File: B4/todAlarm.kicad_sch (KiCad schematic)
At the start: 4 parts, among them U407 74HC377, U408 74HC377, U409 74HC377, U410 74HC377

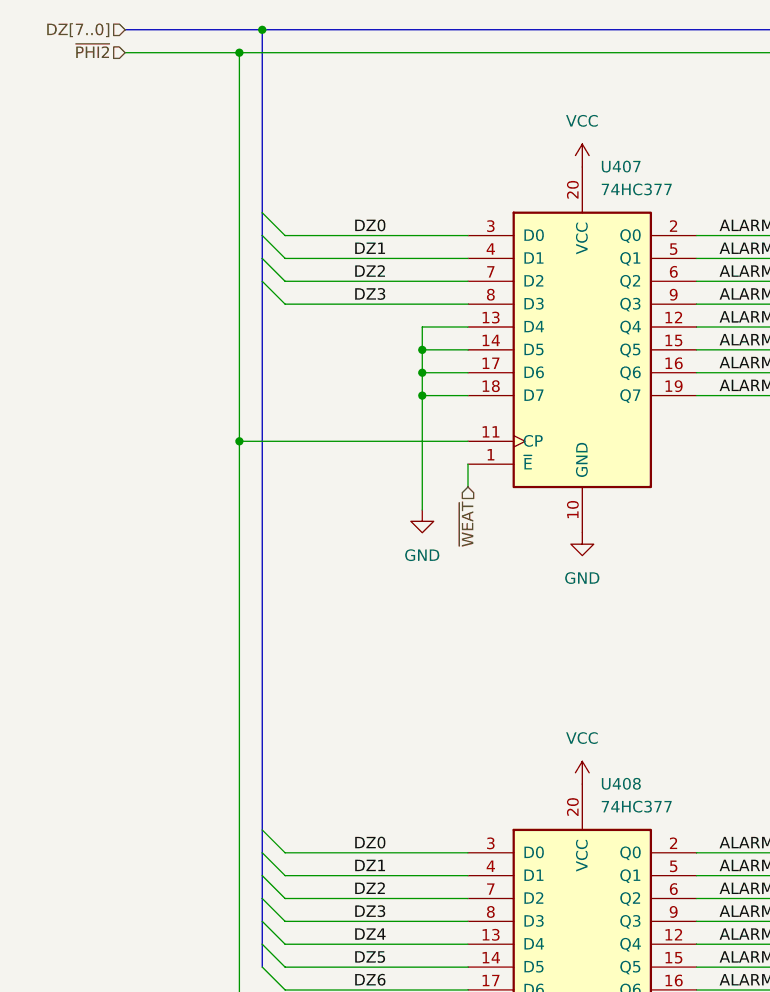
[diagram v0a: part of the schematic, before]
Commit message: B2 refactored. B4 Added. TOD sch completed.
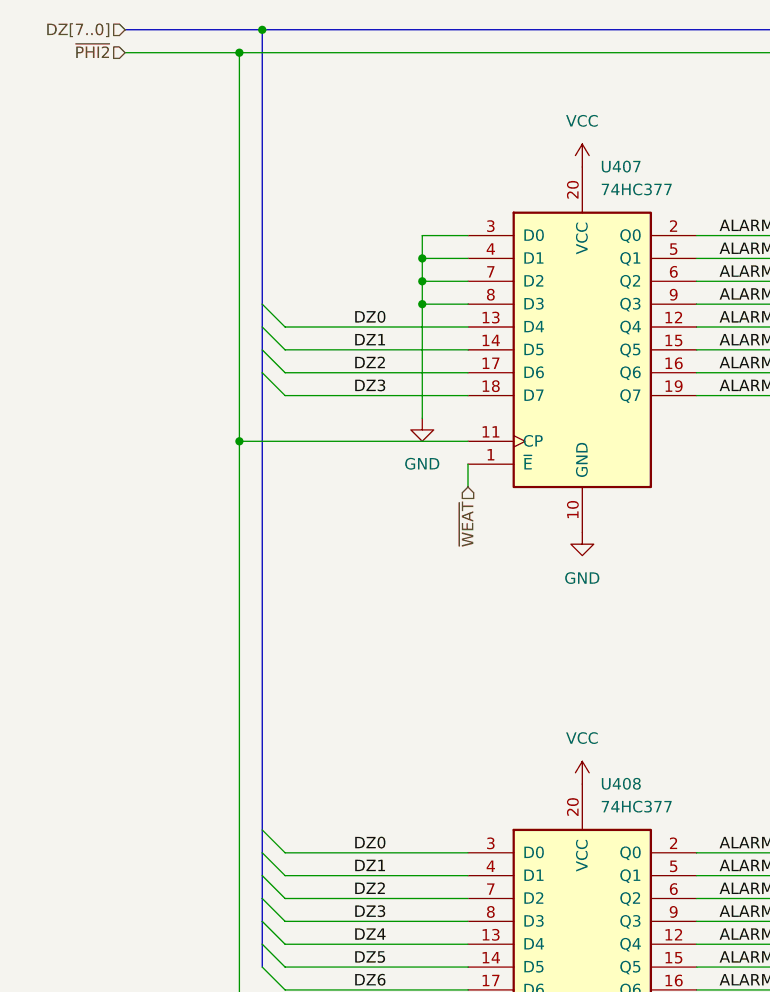
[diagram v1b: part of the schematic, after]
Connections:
- net DZ0: now also U407.13 (D4); no longer U407.3 (D0)
- net DZ1: now also U407.14 (D5); no longer U407.4 (D1)
- net DZ2: now also U407.17 (D6); no longer U407.7 (D2)
- net DZ3: now also U407.18 (D7); no longer U407.8 (D3)
- net GND: now also U407.3 (D0), U407.4 (D1), U407.7 (D2), U407.8 (D3); no longer U407.13 (D4), U407.14 (D5), U407.17 (D6), U407.18 (D7)

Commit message: TOD is here
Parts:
- renumbered U407 to U401
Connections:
- net ALARM0 is gone; now on net ALARM5: U401.2 (Q0)
- net ALARM1 is gone; now on net ALARM4: U401.5 (Q1)
- net ALARM2 is gone; now on net ALARM6: U401.6 (Q2)
- net ALARM3 is gone; now on net ALARM7: U401.9 (Q3)
- net ALARM30 is gone; now on net ALARM28: U410.16 (Q6)
- net ALARM12: now also U409.16 (Q6); no longer U409.12 (Q4)
- net ALARM14: now also U409.12 (Q4); no longer U409.16 (Q6)
- net ALARM16: now also U408.5 (Q1); no longer U408.2 (Q0)
- net ALARM17: now also U408.2 (Q0); no longer U408.5 (Q1)
- net ALARM20: now also U408.16 (Q6); no longer U408.12 (Q4)
- net ALARM22: now also U408.12 (Q4); no longer U408.16 (Q6)
- net ALARM24: now also U410.5 (Q1); no longer U410.2 (Q0)
- net ALARM25: now also U410.2 (Q0); no longer U410.5 (Q1)
- net ALARM28: no longer U410.12 (Q4)
- net ALARM4: no longer U401.12 (Q4)
- net ALARM5: no longer U401.15 (Q5)
- net ALARM6: no longer U401.16 (Q6)
- net ALARM7: no longer U401.19 (Q7)
- net ALARM8: now also U409.5 (Q1); no longer U409.2 (Q0)
- net ALARM9: now also U409.2 (Q0); no longer U409.5 (Q1)
- net DZ0: now also U401.4 (D1), U408.4 (D1), U409.4 (D1), U410.4 (D1); no longer U401.13 (D4), U408.3 (D0), U409.3 (D0), U410.3 (D0)
- net DZ1: now also U401.3 (D0), U408.3 (D0), U409.3 (D0), U410.3 (D0); no longer U401.14 (D5), U408.4 (D1), U409.4 (D1), U410.4 (D1)
- net DZ2: now also U401.7 (D2); no longer U401.17 (D6)
- net DZ3: now also U401.8 (D3); no longer U401.18 (D7)
- net DZ4: now also U408.17 (D6), U409.17 (D6), U410.17 (D6); no longer U408.13 (D4), U409.13 (D4), U410.13 (D4)
- net DZ6: now also U408.13 (D4), U409.13 (D4); no longer U408.17 (D6), U409.17 (D6)
- net GND: now also U401.13 (D4), U401.14 (D5), U401.17 (D6), U401.18 (D7), U410.13 (D4); no longer U401.3 (D0), U401.4 (D1), U401.7 (D2), U401.8 (D3), U410.17 (D6)
- net ALARM15: no longer names the net of U409.19 (Q7)
- net ALARM23: no longer names the net of U408.19 (Q7)
- net ALARM29: no longer names the net of U410.15 (Q5)
- no-connect marks 0 -> 8

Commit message: Ready for v0.2.2
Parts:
- renumbered U401 to U402, U409 to U408, U408 to U413, U410 to U420
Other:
- company: (none) -> Daniel Molina
- title: (none) -> 74HCT6526 Board 4
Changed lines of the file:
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@@
 (kicad_sch (version 20211123) (generator eeschema)
   (paper "A4")
+  (title_block
+    (title "74HCT6526 Board 4")
+    (date "2023-06-22")
+    (rev "0.2.2")
+    (company "Daniel Molina")
+    (comment 1 "https://github.com/dmolinagarcia/74HCT6526")
+  )
   (junction (at 165.1 132.08) (diameter 0) (color 0 0 0 0)
   )
@@
   (symbol (lib_id "74xx:74LS377") (at 182.88 63.5 0) (unit 1)
     (in_bom yes) (on_board yes) (fields_autoplaced)
-    (property "Reference" "U409" (id 0) (at 184.8994 43.18 0)
+    (property "Reference" "U408" (id 0) (at 184.8994 43.18 0)
       (effects (font (size 1.27 1.27)) (justify left))
     )
@@
   (symbol (lib_id "74xx:74LS377") (at 127 132.08 0) (unit 1)
     (in_bom yes) (on_board yes) (fields_autoplaced)
-    (property "Reference" "U408" (id 0) (at 129.0194 111.76 0)
+    (property "Reference" "U413" (id 0) (at 129.0194 111.76 0)
       (effects (font (size 1.27 1.27)) (justify left))
     )
@@
   (symbol (lib_id "74xx:74LS377") (at 127 63.5 0) (unit 1)
     (in_bom yes) (on_board yes) (fields_autoplaced)
-    (property "Reference" "U401" (id 0) (at 129.0194 43.18 0)
+    (property "Reference" "U402" (id 0) (at 129.0194 43.18 0)
       (effects (font (size 1.27 1.27)) (justify left))
     )
@@
   (symbol (lib_id "74xx:74LS377") (at 182.88 132.08 0) (unit 1)
     (in_bom yes) (on_board yes) (fields_autoplaced)
-    (property "Reference" "U410" (id 0) (at 184.8994 111.76 0)
+    (property "Reference" "U420" (id 0) (at 184.8994 111.76 0)
       (effects (font (size 1.27 1.27)) (justify left))
     )
